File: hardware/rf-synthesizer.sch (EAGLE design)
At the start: 78 parts, among them IC1 ATMEGA168-AU, J1 U.FL, U1 ADF4351, U4 MIC5319, X1 10MHz, Y1 12MHz

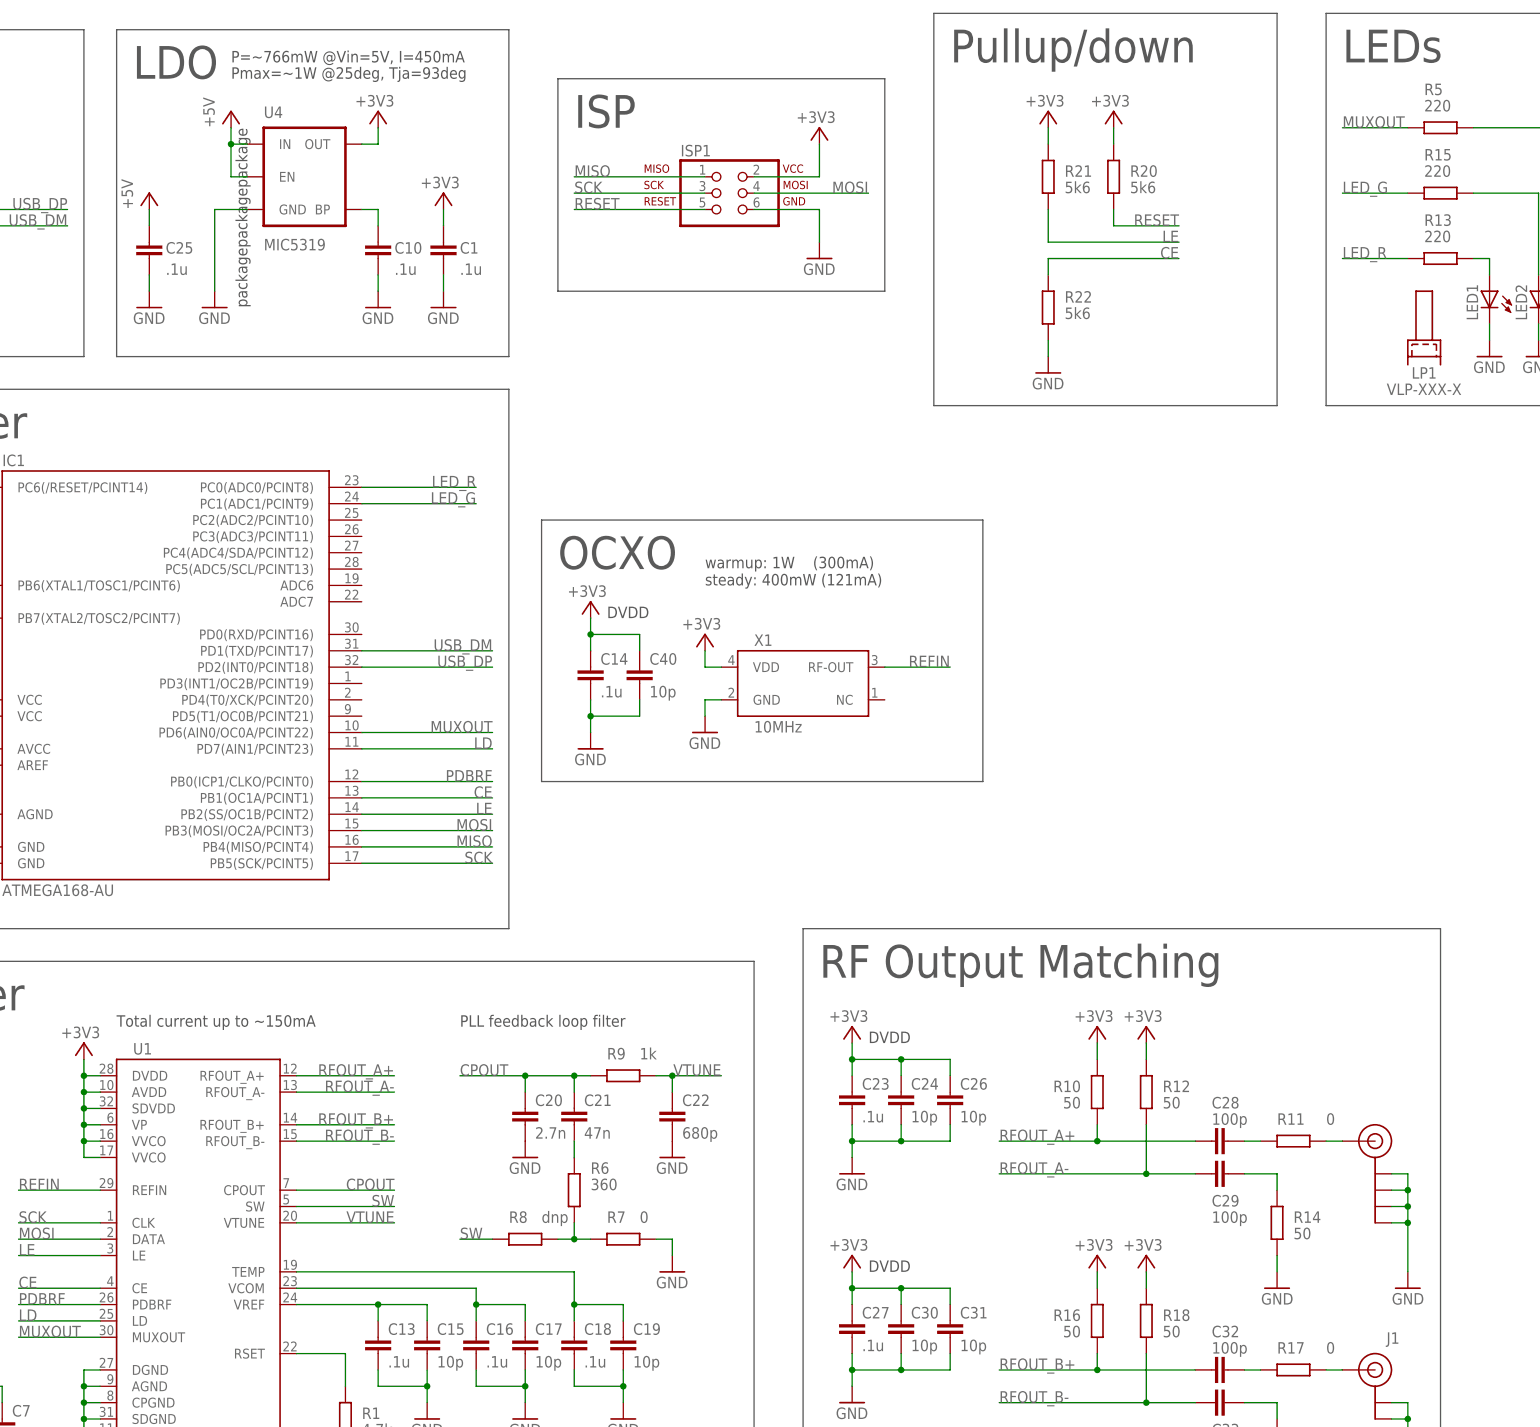
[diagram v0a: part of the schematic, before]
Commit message: sch: almost ready for layout, new refclk and ldo
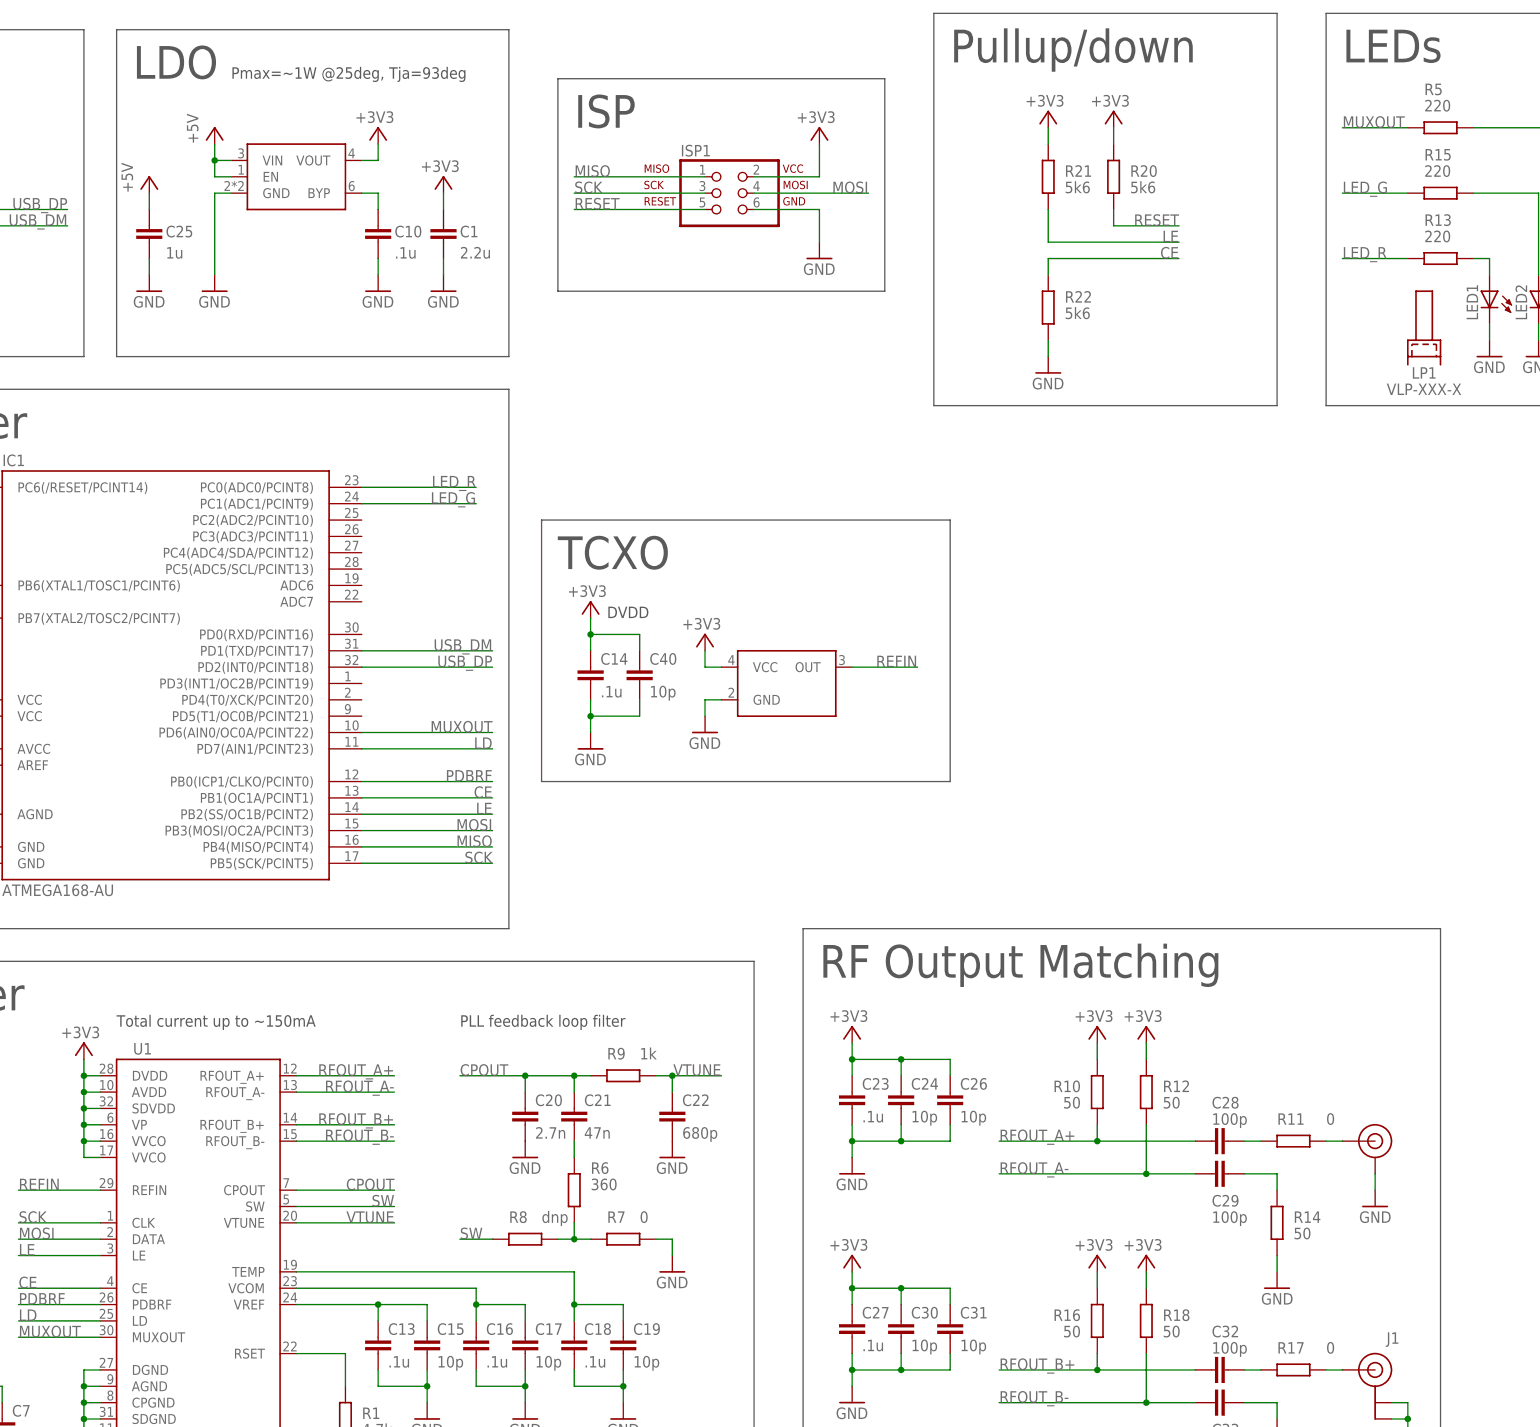
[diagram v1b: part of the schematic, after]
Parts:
- removed J$1: SMA_EDGE, SparkFun-Connectors:SMA_EDGE
- removed U4: MIC5319, SparkFun-PowerIC:V_REG_LDOSMD
- added J$2: SMA_EDGEB, balto:SMA_EDGEB
- added U2: MIC5319, balto:LDO-5PIN
- C1: value .1u -> 2.2u
- C25: value .1u -> 1u
- X1: value 10MHz -> FOX924B-10MHz; device balto:AOCJYR-OCXO -> balto:OSCILLATOR
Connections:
- net +3V3: now also U2.VOUT, X1.VCC; no longer U4.OUT, X1.VDD
- net +5V: now also U2.EN, U2.VIN; no longer U4.EN, U4.IN
- net GND: now also J$2.GND, U2.GND; no longer J$1.GND@0, J$1.GND@1, J$1.GND@2, J$1.GND@3, U4.GND
- net N$8: now also U2.BYP; no longer U4.BP
- net N$9: now also J$2.FEED; no longer J$1.SIGNAL
- net REFIN: now also X1.OUT; no longer X1.RF-OUT
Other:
- note added: "TCXO"
- note removed: "OCXO"
- note removed: "P=~766mW @Vin=5V, I=450mA"
- note removed: "packagepackagepackage"
- note removed: "warmup: 1W (300mA) steady: 400mW (121mA)"
- moved on the sheet: C1, C10, C25

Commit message: brd: layout wip
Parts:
- removed C30, C31: 10p, rcl:C-EUC0603
- removed C32, C33: 100p, rcl:C-EUC0603
- removed R16, R18, R19: 50, rcl:R-EU_R0603
- removed R17: 0, rcl:R-EU_R0603
- removed TP1: TPTP12R, testpad:TPTP12R
- C1, C10, C11, C12, C13, C14, C15, C16, C17, C18, C19, C2, C20, C21, C22, C23, C24, C25, C26, C27, C28, C29, C3, C4, C40, C5, C6, C7, C8, C9: device rcl:C-EUC0603 -> balto:C0603
- C34, C35, C36, C37, C38, C39: device rcl:C-EUC0805 -> balto:C0603
- IC1: value ATMEGA168-AU -> ATMEGA168-MU; device balto:ATMEGA168-AU -> balto:ATMEGA168-MU
- R1, R10, R11, R12, R13, R14, R15, R2, R20, R21, R22, R3, R4, R5, R6, R7, R8, R9: device rcl:R-EU_R0603 -> balto:R0603
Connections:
- net +3V1 renamed VREF
- net +3V2 renamed VCOM
- net +3V4 renamed TEMP
- removed net N$10: C29.2, R14.1
- removed net N$11: C32.2, R17.1
- removed net N$13: C33.2, R19.1
- net +3V3: now also R2.1; no longer C30.1, C31.1, R16.1, R18.1, R2.2
- net GND: no longer C30.2, C31.2, R19.2
- net LD: now also IC1.PC2(ADC2/PCINT10); no longer IC1.PD7(AIN1/PCINT23)
- net LED_G: now also IC1.PC3(ADC3/PCINT11); no longer IC1.PC1(ADC1/PCINT9)
- net LED_R: now also IC1.PC4(ADC4/SDA/PCINT12); no longer IC1.PC0(ADC0/PCINT8)
- net MUXOUT: now also IC1.PC0(ADC0/PCINT8); no longer IC1.PD6(AIN0/OC0A/PCINT22), TP1.TP
- net N$1: now also R3.1; no longer R4.2
- net N$12: now also C29.2, R14.1; no longer R17.2
- net N$7: now also R2.2, R4.1; no longer R2.1, R3.2
- net PDBRF: now also IC1.PC1(ADC1/PCINT9); no longer IC1.PB0(ICP1/CLKO/PCINT0)
- net RFOUT_B+: no longer C32.1, R16.2
- net RFOUT_B-: no longer C33.1, R18.2
- net USB_DM: now also R4.2; no longer R3.1
- net USB_DP: now also R3.2; no longer R4.1
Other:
- moved on the sheet: C23, C24, C26, C27, IC1, J1, R14, R2, R3, R4

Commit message: brd: fully routed
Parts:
- removed LED3: (no value), led:LEDSML0805
- removed LP2: VLP-XXX-X, balto:VLP-XXX-X
- removed R5: 220, balto:R0603
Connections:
- removed net N$16: LED3.A, R5.1
- removed net N$23: LED2.A, R15.1
- removed net RFOUT_B+: U1.RFOUT_B+
- removed net RFOUT_B-: U1.RFOUT_B-
- new net N$10: LED2.C, R15.2
- net GND: now also R13.1, R15.1; no longer LED1.C, LED2.C, LED3.C
- net LED_G: now also LED2.A; no longer R15.2
- net LED_R: now also LED1.A; no longer R13.2
- net MUXOUT: no longer R5.2
- net N$3: now also LED1.C, R13.2; no longer LED1.A, R13.1
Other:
- moved on the sheet: LED1, LED2, R13, R15

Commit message: hw: add a comment about assembly stuff
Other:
- note added: "470//1k5"
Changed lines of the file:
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@@
 <?xml version="1.0" encoding="utf-8"?>
 <!DOCTYPE eagle SYSTEM "eagle.dtd">
-<eagle version="7.3.0">
+<eagle version="7.5.0">
 <drawing>
 <settings>
@@
 <text x="71.12" y="101.6" size="1.778" layer="97">Total current up to ~150mA</text>
 <text x="88.9" y="248.92" size="1.778" layer="97">Pmax=~1W @25deg, Tja=93deg</text>
+<text x="144.78" y="73.66" size="1.778" layer="97">470//1k5</text>
 </plain>
 <instances>
